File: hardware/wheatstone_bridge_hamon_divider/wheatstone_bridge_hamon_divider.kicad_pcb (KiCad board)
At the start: 2 copper layers, 100 x 100 mm, 2 parts

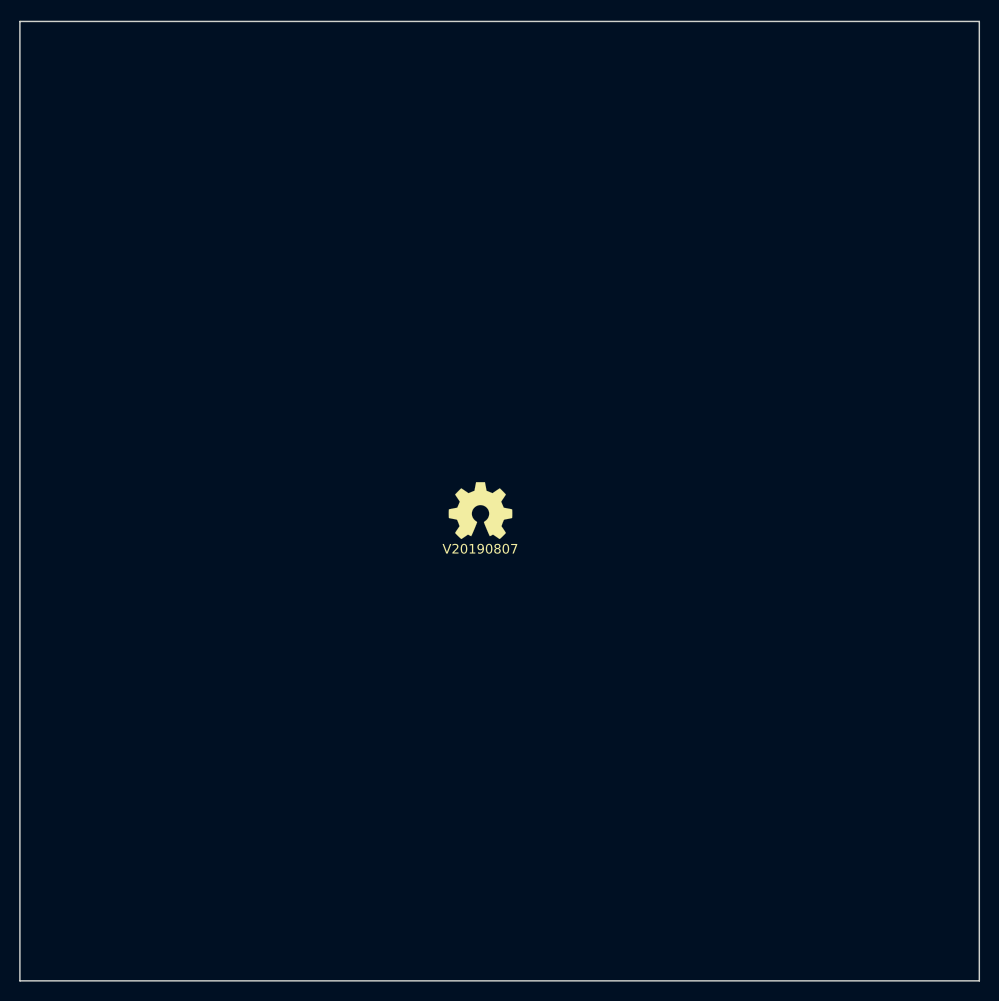
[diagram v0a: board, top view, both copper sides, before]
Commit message: added mounting holes and case net
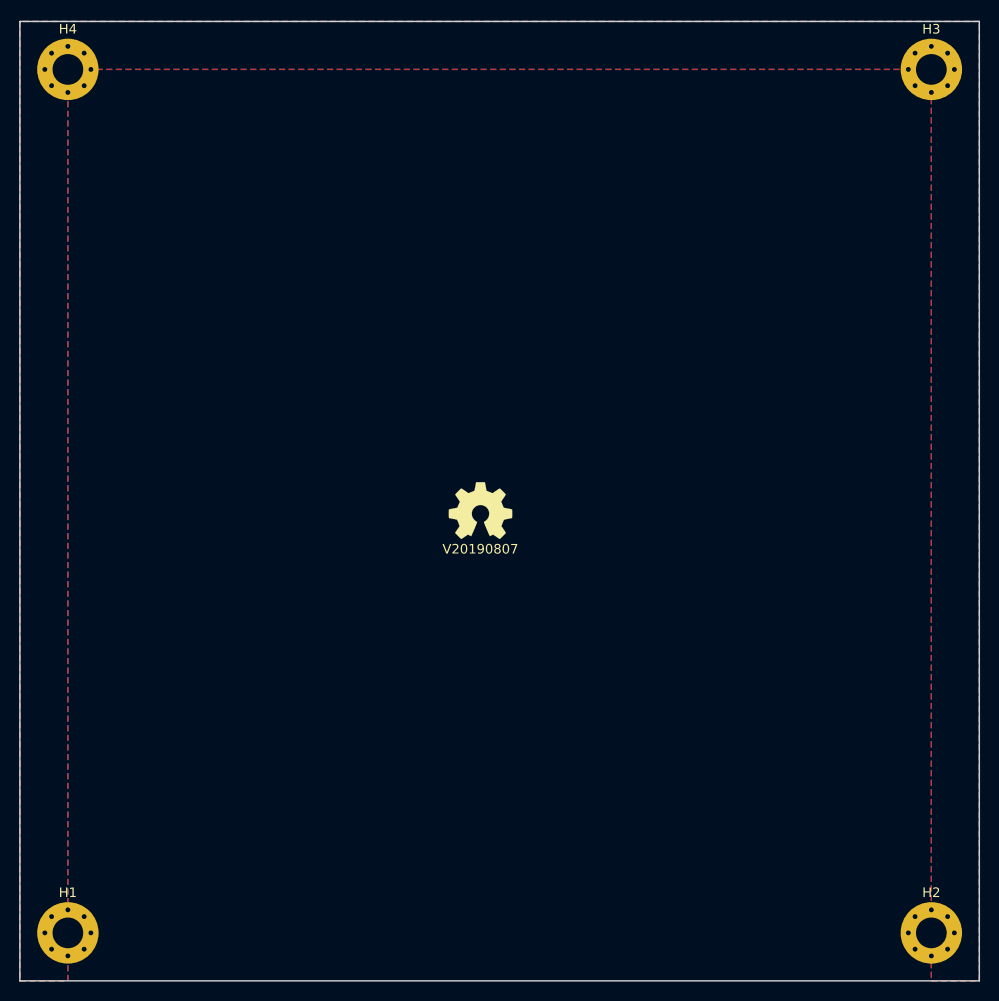
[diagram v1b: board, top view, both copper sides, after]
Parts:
- added H1: MountingHole_Pad, Mounting_Holes:MountingHole_3.2mm_M3_Pad_Via, F.Cu at (105.0, 145.0)
- added H2: MountingHole_Pad, Mounting_Holes:MountingHole_3.2mm_M3_Pad_Via, F.Cu at (195.0, 145.0)
- added H3: MountingHole_Pad, Mounting_Holes:MountingHole_3.2mm_M3_Pad_Via, F.Cu at (195.0, 55.0)
- added H4: MountingHole_Pad, Mounting_Holes:MountingHole_3.2mm_M3_Pad_Via, F.Cu at (105.0, 55.0)
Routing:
- added copper zone on B.Cu, net /CASE
- added copper zone on F.Cu, net /CASE
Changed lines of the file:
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@@
     (tracks 0)
     (zones 0)
-    (modules 2)
-    (nets 1)
+    (modules 6)
+    (nets 2)
   )
   (page A4)
@@
   )
   (net 0 "")
+  (net 1 /CASE)
   (net_class Default "This is the default net class."
     (clearance 0.127)
@@
     (uvia_dia 0.6)
     (uvia_drill 0.3)
+    (add_net /CASE)
+  )
+  (module Mounting_Holes:MountingHole_3.2mm_M3_Pad_Via (layer F.Cu)
+    (at 105 55)
+    (descr "Mounting Hole 3.2mm, M3")
+    (tags "mounting hole 3.2mm m3")
+    (attr virtual)
+    (fp_text reference H4 (at 0 -4.2) (layer F.SilkS)
+      (effects (font (size 1 1) (thickness 0.15)))
+    )
+    (fp_text value MountingHole_Pad (at 0 4.2) (layer F.Fab)
+      (effects (font (size 1 1) (thickness 0.15)))
+    )
+    (fp_text user %R (at 0.3 0) (layer F.Fab)
+      (effects (font (size 1 1) (thickness 0.15)))
+    )
+    (fp_circle (center 0 0) (end 3.2 0) (layer Cmts.User) (width 0.15))
+    (fp_circle (center 0 0) (end 3.45 0) (layer F.CrtYd) (width 0.05))
+    (pad 1 thru_hole circle (at 0 0) (size 6.4 6.4) (drill 3.2) (layers *.Cu *.Mask)
+      (net 1 /CASE))
+    (pad 1 thru_hole circle (at 2.4 0) (size 0.8 0.8) (drill 0.5) (layers *.Cu *.Mask)
+      (net 1 /CASE))
+    (pad 1 thru_hole circle (at 1.697056 1.697056) (size 0.8 0.8) (drill 0.5) (layers *.Cu *.Mask)
+      (net 1 /CASE))
+    (pad 1 thru_hole circle (at 0 2.4) (size 0.8 0.8) (drill 0.5) (layers *.Cu *.Mask)
+      (net 1 /CASE))
+    (pad 1 thru_hole circle (at -1.697056 1.697056) (size 0.8 0.8) (drill 0.5) (layers *.Cu *.Mask)
+      (net 1 /CASE))
+    (pad 1 thru_hole circle (at -2.4 0) (size 0.8 0.8) (drill 0.5) (layers *.Cu *.Mask)
+      (net 1 /CASE))
+    (pad 1 thru_hole circle (at -1.697056 -1.697056) (size 0.8 0.8) (drill 0.5) (layers *.Cu *.Mask)
+      (net 1 /CASE))
+    (pad 1 thru_hole circle (at 0 -2.4) (size 0.8 0.8) (drill 0.5) (layers *.Cu *.Mask)
+      (net 1 /CASE))
+    (pad 1 thru_hole circle (at 1.697056 -1.697056) (size 0.8 0.8) (drill 0.5) (layers *.Cu *.Mask)
+      (net 1 /CASE))
+  )
+  (module Mounting_Holes:MountingHole_3.2mm_M3_Pad_Via (layer F.Cu)
+    (at 195 55)
+    (descr "Mounting Hole 3.2mm, M3")
+    (tags "mounting hole 3.2mm m3")
+    (attr virtual)
+    (fp_text reference H3 (at 0 -4.2) (layer F.SilkS)
+      (effects (font (size 1 1) (thickness 0.15)))
+    )
+    (fp_text value MountingHole_Pad (at 0 4.2) (layer F.Fab)
+      (effects (font (size 1 1) (thickness 0.15)))
+    )
+    (fp_text user %R (at 0.3 0) (layer F.Fab)
+      (effects (font (size 1 1) (thickness 0.15)))
+    )
+    (fp_circle (center 0 0) (end 3.2 0) (layer Cmts.User) (width 0.15))
+    (fp_circle (center 0 0) (end 3.45 0) (layer F.CrtYd) (width 0.05))
+    (pad 1 thru_hole circle (at 0 0) (size 6.4 6.4) (drill 3.2) (layers *.Cu *.Mask)
+      (net 1 /CASE))
+    (pad 1 thru_hole circle (at 2.4 0) (size 0.8 0.8) (drill 0.5) (layers *.Cu *.Mask)
+      (net 1 /CASE))
+    (pad 1 thru_hole circle (at 1.697056 1.697056) (size 0.8 0.8) (drill 0.5) (layers *.Cu *.Mask)
+      (net 1 /CASE))
+    (pad 1 thru_hole circle (at 0 2.4) (size 0.8 0.8) (drill 0.5) (layers *.Cu *.Mask)
+      (net 1 /CASE))
+    (pad 1 thru_hole circle (at -1.697056 1.697056) (size 0.8 0.8) (drill 0.5) (layers *.Cu *.Mask)
+      (net 1 /CASE))
+    (pad 1 thru_hole circle (at -2.4 0) (size 0.8 0.8) (drill 0.5) (layers *.Cu *.Mask)
+      (net 1 /CASE))
+    (pad 1 thru_hole circle (at -1.697056 -1.697056) (size 0.8 0.8) (drill 0.5) (layers *.Cu *.Mask)
+      (net 1 /CASE))
+    (pad 1 thru_hole circle (at 0 -2.4) (size 0.8 0.8) (drill 0.5) (layers *.Cu *.Mask)
+      (net 1 /CASE))
+    (pad 1 thru_hole circle (at 1.697056 -1.697056) (size 0.8 0.8) (drill 0.5) (layers *.Cu *.Mask)
+      (net 1 /CASE))
+  )
+  (module Mounting_Holes:MountingHole_3.2mm_M3_Pad_Via (layer F.Cu)
+    (at 195 145)
+    (descr "Mounting Hole 3.2mm, M3")
+    (tags "mounting hole 3.2mm m3")
+    (attr virtual)
+    (fp_text reference H2 (at 0 -4.2) (layer F.SilkS)
+      (effects (font (size 1 1) (thickness 0.15)))
+    )
+    (fp_text value MountingHole_Pad (at 0 4.2) (layer F.Fab)
+      (effects (font (size 1 1) (thickness 0.15)))
+    )
+    (fp_text user %R (at 0.3 0) (layer F.Fab)
+      (effects (font (size 1 1) (thickness 0.15)))
+    )
+    (fp_circle (center 0 0) (end 3.2 0) (layer Cmts.User) (width 0.15))
+    (fp_circle (center 0 0) (end 3.45 0) (layer F.CrtYd) (width 0.05))
+    (pad 1 thru_hole circle (at 0 0) (size 6.4 6.4) (drill 3.2) (layers *.Cu *.Mask)
+      (net 1 /CASE))
+    (pad 1 thru_hole circle (at 2.4 0) (size 0.8 0.8) (drill 0.5) (layers *.Cu *.Mask)
+      (net 1 /CASE))
+    (pad 1 thru_hole circle (at 1.697056 1.697056) (size 0.8 0.8) (drill 0.5) (layers *.Cu *.Mask)
+      (net 1 /CASE))
+    (pad 1 thru_hole circle (at 0 2.4) (size 0.8 0.8) (drill 0.5) (layers *.Cu *.Mask)
+      (net 1 /CASE))
+    (pad 1 thru_hole circle (at -1.697056 1.697056) (size 0.8 0.8) (drill 0.5) (layers *.Cu *.Mask)
+      (net 1 /CASE))
+    (pad 1 thru_hole circle (at -2.4 0) (size 0.8 0.8) (drill 0.5) (layers *.Cu *.Mask)
+      (net 1 /CASE))
+    (pad 1 thru_hole circle (at -1.697056 -1.697056) (size 0.8 0.8) (drill 0.5) (layers *.Cu *.Mask)
+      (net 1 /CASE))
+    (pad 1 thru_hole circle (at 0 -2.4) (size 0.8 0.8) (drill 0.5) (layers *.Cu *.Mask)
+      (net 1 /CASE))
+    (pad 1 thru_hole circle (at 1.697056 -1.697056) (size 0.8 0.8) (drill 0.5) (layers *.Cu *.Mask)
+      (net 1 /CASE))
+  )
+  (module Mounting_Holes:MountingHole_3.2mm_M3_Pad_Via (layer F.Cu)
+    (at 105 145)
+    (descr "Mounting Hole 3.2mm, M3")
+    (tags "mounting hole 3.2mm m3")
+    (attr virtual)
+    (fp_text reference H1 (at 0 -4.2) (layer F.SilkS)
+      (effects (font (size 1 1) (thickness 0.15)))
+    )
+    (fp_text value MountingHole_Pad (at 0 4.2) (layer F.Fab)
+      (effects (font (size 1 1) (thickness 0.15)))
+    )
+    (fp_text user %R (at 0.3 0) (layer F.Fab)
+      (effects (font (size 1 1) (thickness 0.15)))
+    )
+    (fp_circle (center 0 0) (end 3.2 0) (layer Cmts.User) (width 0.15))
+    (fp_circle (center 0 0) (end 3.45 0) (layer F.CrtYd) (width 0.05))
+    (pad 1 thru_hole circle (at 0 0) (size 6.4 6.4) (drill 3.2) (layers *.Cu *.Mask)
+      (net 1 /CASE))
+    (pad 1 thru_hole circle (at 2.4 0) (size 0.8 0.8) (drill 0.5) (layers *.Cu *.Mask)
+      (net 1 /CASE))
+    (pad 1 thru_hole circle (at 1.697056 1.697056) (size 0.8 0.8) (drill 0.5) (layers *.Cu *.Mask)
+      (net 1 /CASE))
+    (pad 1 thru_hole circle (at 0 2.4) (size 0.8 0.8) (drill 0.5) (layers *.Cu *.Mask)
+      (net 1 /CASE))
+    (pad 1 thru_hole circle (at -1.697056 1.697056) (size 0.8 0.8) (drill 0.5) (layers *.Cu *.Mask)
+      (net 1 /CASE))
+    (pad 1 thru_hole circle (at -2.4 0) (size 0.8 0.8) (drill 0.5) (layers *.Cu *.Mask)
+      (net 1 /CASE))
+    (pad 1 thru_hole circle (at -1.697056 -1.697056) (size 0.8 0.8) (drill 0.5) (layers *.Cu *.Mask)
+      (net 1 /CASE))
+    (pad 1 thru_hole circle (at 0 -2.4) (size 0.8 0.8) (drill 0.5) (layers *.Cu *.Mask)
+      (net 1 /CASE))
+    (pad 1 thru_hole circle (at 1.697056 -1.697056) (size 0.8 0.8) (drill 0.5) (layers *.Cu *.Mask)
+      (net 1 /CASE))
   )
   (module Symbols:OSHW-Symbol_6.7x6mm_SilkScreen (layer F.Cu)
@@
   (gr_line (start 200 150) (end 100 150) (layer Edge.Cuts) (width 0.15))
   (gr_line (start 100 50) (end 200 50) (layer Edge.Cuts) (width 0.15))
+  (zone (net 1) (net_name /CASE) (layer B.Cu) (hatch edge 0.508)
+    (connect_pads (clearance 0.508))
+    (min_thickness 0.254)
+    (fill yes (arc_segments 32) (thermal_gap 0.508) (thermal_bridge_width 0.508))
+    (polygon
+      (pts
+        (xy 105 150) (xy 105 55) (xy 195 55) (xy 195 150) (xy 200 150)
+        (xy 200 50) (xy 100 50) (xy 100 150)
+      )
+    )
+  )
+  (zone (net 1) (net_name /CASE) (layer F.Cu) (hatch edge 0.508)
+    (connect_pads (clearance 0.508))
+    (min_thickness 0.254)
+    (fill yes (arc_segments 32) (thermal_gap 0.508) (thermal_bridge_width 0.508))
+    (polygon
+      (pts
+        (xy 100 150) (xy 105 150) (xy 105 55) (xy 195 55) (xy 195 150)
+        (xy 200 150) (xy 200 50) (xy 100 50)
+      )
+    )
+  )
 )
